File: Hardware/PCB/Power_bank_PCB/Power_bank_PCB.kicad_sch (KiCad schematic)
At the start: 0 parts

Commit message: Add battery protection and control schematic
Adds the custom 8205A MOSFET symbol and KiCad project metadata generated by the PCB editor, plus updates to the Power_bank_PCB schematic with the battery charger, protection, switching, MCU, and INA219 monitoring blocks. Also includes backup ZIPs and lockfile cleanup for the project.
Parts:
- added C1: C_Polarized, symbol Device:C_Polarized
- added C2: 0.1u, symbol Device:C
- added J1: Fotopanel_connector, symbol Connector:Screw_Terminal_01x02
- added Q1: 8205A, Package_SO:TSSOP-8_4.4x3mm_P0.65mm, symbol 8205A:8205A
- added Q2: 2N7002, Package_TO_SOT_SMD:SOT-23, symbol Transistor_FET:2N7002
- added Q3: DMP3099L, Package_TO_SOT_SMD:SOT-23, symbol Transistor_FET:DMP3099L
- added R1, R2: 10k, symbol Device:R
- added R3: 0.05, symbol Device:R
- added TP1: SWDIO, Connector_Pin:Pin_D1.3mm_L11.0mm_LooseFit, symbol Connector:TestPoint
- added TP2: SWCLK, Connector_Pin:Pin_D1.3mm_L11.0mm_LooseFit, symbol Connector:TestPoint
- added U1: TP4056-42-ESOP8, Package_SO:SOIC-8-1EP_3.9x4.9mm_P1.27mm_EP2.41x3.3mm_ThermalVias, symbol Battery_Management:TP4056-42-ESOP8
- added U2: XL4015, Package_TO_SOT_SMD:TO-263-5_TabPin3, symbol Regulator_Switching:XL4015
- added U3: MCP4018-xxxxLT, Package_TO_SOT_SMD:SOT-363_SC-70-6, symbol Potentiometer_Digital:MCP4018-xxxxLT
- added U4: DW01A, Package_TO_SOT_SMD:SOT-23-6, symbol Battery_Management:DW01A
- added U5: STM32U031F8Px, Package_SO:TSSOP-20_4.4x6.5mm_P0.65mm, symbol MCU_ST_STM32U0:STM32U031F8Px
- added U6: INA219AxD, Package_SO:SOIC-8_3.9x4.9mm_P1.27mm, symbol Sensor_Energy:INA219AxD
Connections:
- new net: Q3.2 (S), R2.1, R3.2, U6.7 (IN-)
- new net: J1.2 (Pin_2), R3.1, U6.8 (IN+)
- new net: TP1.1, U5.17 (PA13)
- new net: Q2.3 (D), Q3.1 (G), R2.2
- new net: TP2.1, U5.18 (PA14/PB4/PB5/PB6)
- new net +3.3V: C2.2, U6.5 (VS)
- new net Fotopanel_switch: Q2.1 (G), R1.1
- new net GND: C2.1, J1.1 (Pin_1), Q2.2 (S), R1.2, U6.1 (A1), U6.2 (A0), U6.6 (GND)
- new net SCL: U6.4 (SCL)
- new net SDA: U6.3 (SDA)
- new net Vfoto: Q3.3 (D)

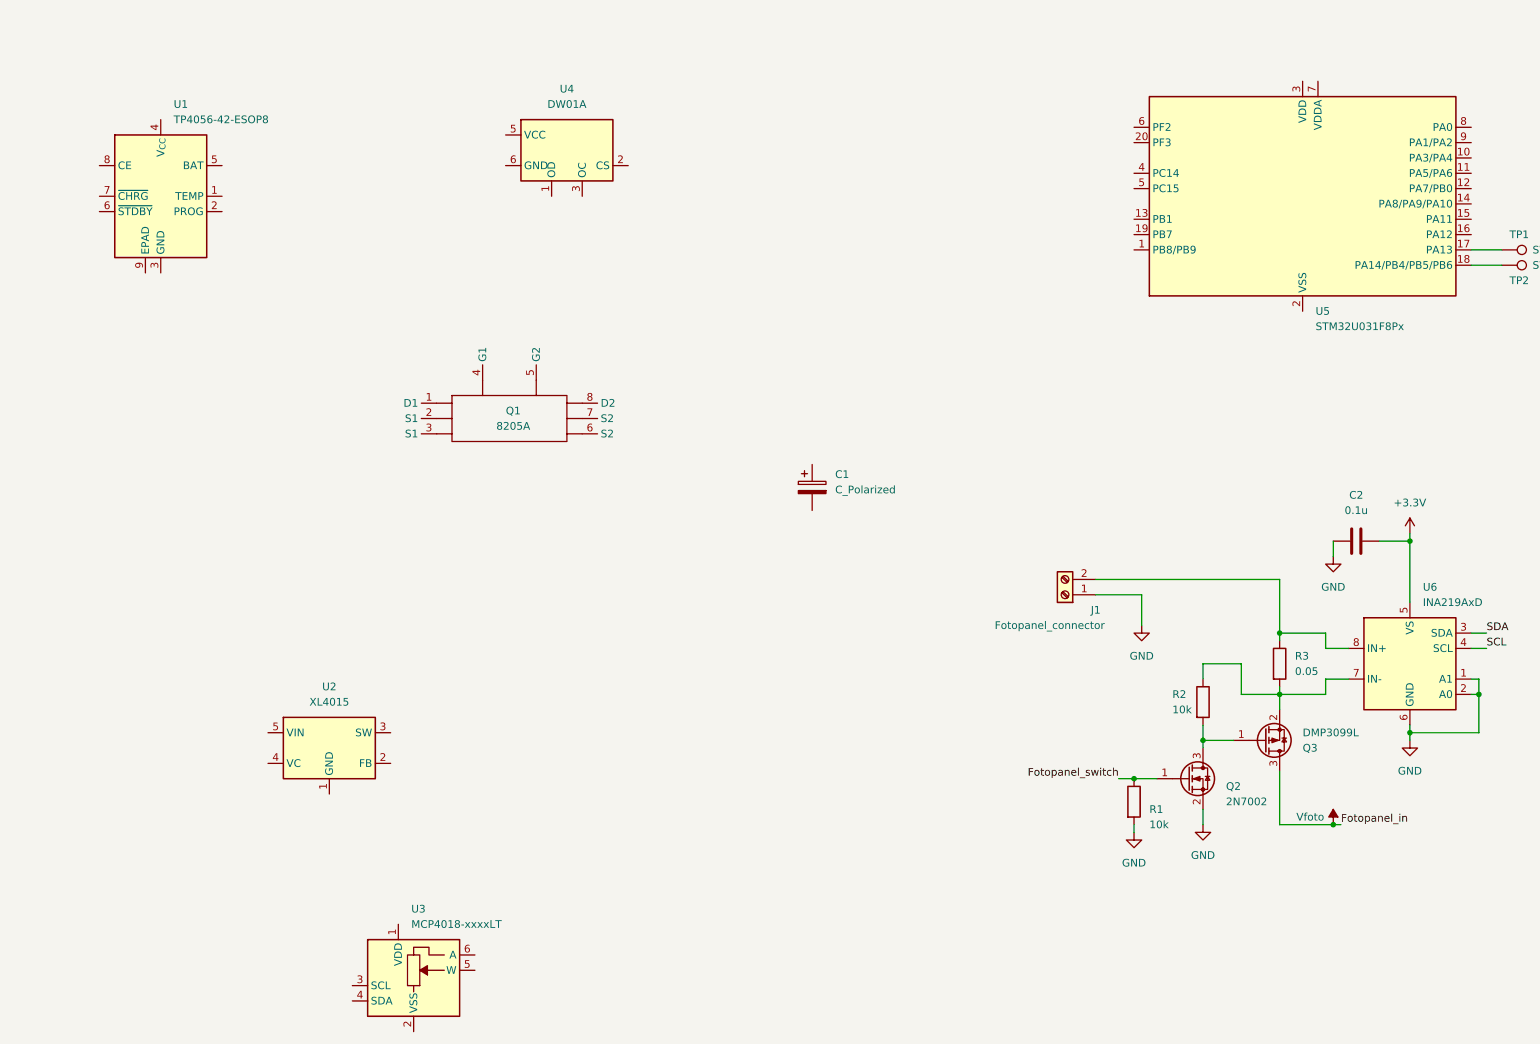
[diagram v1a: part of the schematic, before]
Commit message: Update of BMS, not finished
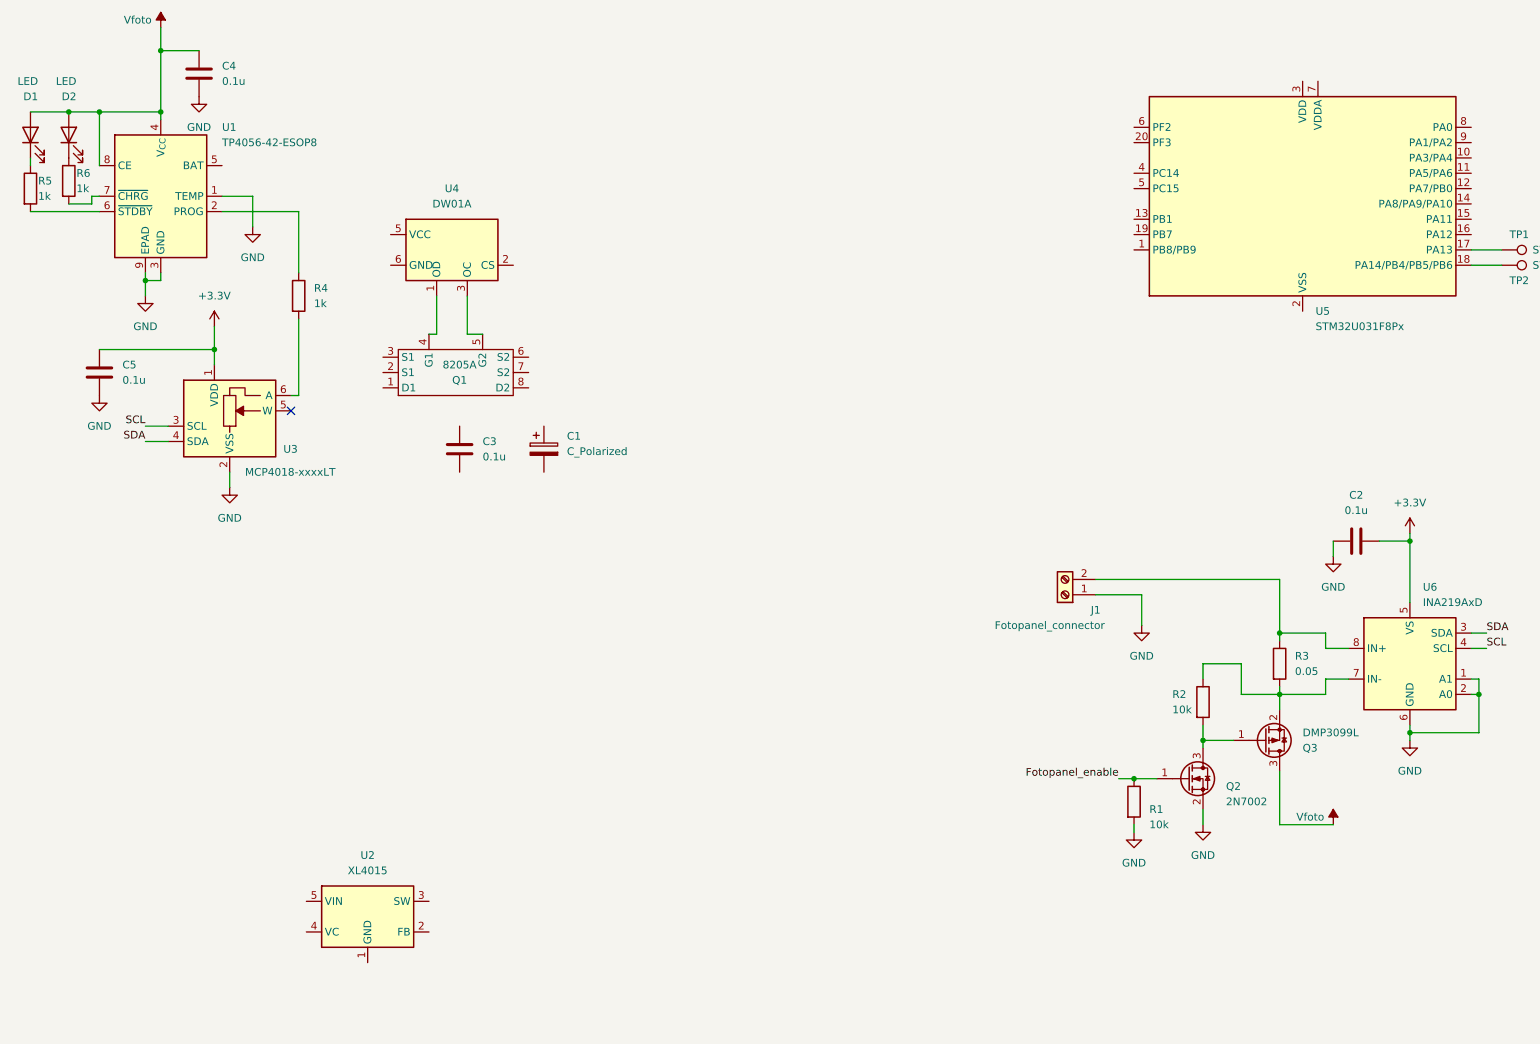
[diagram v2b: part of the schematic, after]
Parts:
- added C3, C4, C5: 0.1u, symbol Device:C
- added D1, D2: LED, symbol Device:LED
- added R4, R5, R6: 1k, symbol Device:R
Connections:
- net +3.3V: now also U3.1 (VDD), C5.1
- net GND: now also U1.1 (TEMP), U1.3 (GND), U1.9 (EPAD), U3.2 (VSS), C4.2, C5.2
- net SCL: now also U3.3 (SCL)
- net SDA: now also U3.4 (SDA)
- net Vfoto: now also U1.4 (V_{CC}), U1.8 (CE), C4.1, D1.2 (A), D2.2 (A)
- net at U4.1 (OD): now also Q1.4 (G1)
- net at U4.3 (OC): now also Q1.5 (G2)
- net at U1.2 (PROG): now also R4.1
- net at U1.6 (~{STDBY}): now also R5.2
- net at U1.7 (~{CHRG}): now also R6.2
- net at U3.6 (A): now also R4.2
- net Fotopanel_switch renamed Fotopanel_enable
- new net: D1.1 (K), R5.1
- new net: D2.1 (K), R6.1
- no-connect marks 0 -> 1
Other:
- moved on the sheet: C1, U2, U3, U4

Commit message: Update of schematic
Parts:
- removed U2: XL4015, Package_TO_SOT_SMD:TO-263-5_TabPin3, symbol Regulator_Switching:XL4015
- added C6: 680u, symbol Device:C_Polarized
- added C7: 0.1u, symbol Device:C
- added C8: 22u, symbol Device:C
- added C9: 220u, symbol Device:C_Polarized
- added D3: SS23, Diode_SMD:D_SMA, symbol Diode:SS23
- added L1: 33uH / 3A, symbol Device:L
- added L2: 4.7uH / 1.5A, symbol Device:L
- added R7: 100, symbol Device:R
- added R8: 1k, symbol Device:R
- added TP3: Vbat, Connector_Pin:Pin_D1.3mm_L11.0mm_LooseFit, symbol Connector:TestPoint
- added TP4: Bat-, Connector_Pin:Pin_D1.3mm_L11.0mm_LooseFit, symbol Connector:TestPoint
- added U7: LM2596S-5, Package_TO_SOT_SMD:TO-263-5_TabPin3, symbol Regulator_Switching:LM2596S-5
- added U8: TPS613221ADBV, Package_TO_SOT_SMD:SOT-23-5, symbol Regulator_Switching:TPS613221ADBV
- C1: value C_Polarized -> 10u
- C4: value 0.1u -> 10u
- R4: value 1k -> 3k
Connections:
- net +3.3V: now also C8.1, U8.4 (VOUT)
- net GND: now also C1.2, Q1.6 (S2), Q1.7 (S2), U3.5 (W), C6.2, C7.2, C8.2, C9.2, D3.2 (A), R8.2, U7.3 (GND), U7.5 (~{ON}/OFF), U8.2 (GND)
- net Vfoto: now also C6.1, C7.1, U7.1 (VIN); no longer C4.1, D1.2 (A), D2.2 (A), U1.4 (V_{CC}), U1.8 (CE)
- net at U4.2 (CS): now also R8.1
- net at U4.5 (VCC): now also C3.2, R7.2
- net Bat-: now reaches U4.6 (GND)
- net Bat-: now also C3.1, Q1.2 (S1), Q1.3 (S1), TP4.1
- net Vbat: now reaches U1.5 (BAT)
- net Vbat: now also C1.1, L2.1, R7.1, TP3.1
- net at Q1.1 (D1): now also Q1.8 (D2)
- new net: D3.1 (K), L1.1, U7.2 (OUT)
- new net: L2.2, U8.1 (SW)
- new net Vcharge: C4.1, C9.1, D1.2 (A), D2.2 (A), L1.2, U1.4 (V_{CC}), U1.8 (CE), U7.4 (FB)
- no-connect marks 1 -> 0
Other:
- note added: "find and replace to buck-boost converter!!"
- moved on the sheet: C1, C2, C3, J1, Q1, Q2, Q3, R1, R2, R3, U4, U6

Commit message: Finishing schematic
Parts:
- removed C6: 680u, symbol Device:C_Polarized
- removed C8: 22u, symbol Device:C
- removed C9: 220u, symbol Device:C_Polarized
- removed D3: SS23, Diode_SMD:D_SMA, symbol Diode:SS23
- removed U7: LM2596S-5, Package_TO_SOT_SMD:TO-263-5_TabPin3, symbol Regulator_Switching:LM2596S-5
- removed U8: TPS613221ADBV, Package_TO_SOT_SMD:SOT-23-5, symbol Regulator_Switching:TPS613221ADBV
- added C10, C12, C14, C3, C5: 22u, symbol Device:C
- added C13, C15, C16, C17, C18, C19, C20, C6: 10u, symbol Device:C
- added C2, C21, C22, C23, C9: 100n, symbol Device:C
- added C24: 4.7u, symbol Device:C
- added C25: 1u, symbol Device:C
- added C26: 10n, symbol Device:C
- added IC1, IC2: TPS63070RNMR, KiCad:TPS630701RNMR, symbol TPS63070RNMR:TPS63070RNMR
- added R10, R15, R6: 10k, symbol Device:R
- added R12, R16, R17: 470k, symbol Device:R
- added R13: 150k, symbol Device:R
- added R14, R8: 100k, symbol Device:R
- added R3: 680k, symbol Device:R
- added R4: 130k, symbol Device:R
- added R7: 20k, symbol Device:R
- added TP10: User_button+, Connector_Pin:Pin_D1.3mm_L11.0mm_LooseFit, symbol Connector:TestPoint
- added TP3: Green_LED, Connector_Pin:Pin_D1.3mm_L11.0mm_LooseFit, symbol Connector:TestPoint
- added TP4: Leds_common_GND, Connector_Pin:Pin_D1.3mm_L11.0mm_LooseFit, symbol Connector:TestPoint
- added TP5: User_button-, Connector_Pin:Pin_D1.3mm_L11.0mm_LooseFit, symbol Connector:TestPoint
- added TP8: Red_LED, Connector_Pin:Pin_D1.3mm_L11.0mm_LooseFit, symbol Connector:TestPoint
- added TP9: Yellow_LED, Connector_Pin:Pin_D1.3mm_L11.0mm_LooseFit, symbol Connector:TestPoint
- L1: value 33uH / 3A -> 1.5uH
- L2: value 4.7uH / 1.5A -> 1.5uH
- renumbered C5 to C1, C1 to C11, C2 to C27, C3 to C8, R5 to R1, R8 to R11, R1 to R18, R2 to R19, R6 to R2, R3 to R20, R4 to R5, R7 to R9, TP4 to TP1, TP3 to TP2, TP1 to TP6, TP2 to TP7, U3 to U2, U4 to U3, U5 to U4, U6 to U5
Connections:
- net +3.3V: now also U4.3 (VDD), U4.7 (VDDA), C10.2, C12.2, C14.2, C17.2, C21.2, C22.2, C23.2, C24.2, C25.2, C26.2, IC2.7 (VOUT_1), IC2.8 (VOUT_2), R12.1, R14.2, R16.1, R17.1
- net Fotopanel_enable: now also U4.10 (PA3/PA4)
- net GND: now also U4.2 (VSS), C10.1, C12.1, C13.1, C14.1, C15.1, C16.1, C17.1, C18.1, C19.1, C2.1, C20.1, C21.1, C22.1, C23.1, C24.1, C25.1, C26.1, C3.1, C5.1, C6.1, C9.1, IC1.10 (PGND), IC1.15 (VSEL), IC1.4 (GND), IC1.6 (FB2), IC2.10 (PGND), IC2.15 (VSEL), IC2.4 (GND), IC2.6 (FB2), R13.2, R4.2, R7.2, TP4.1, TP5.1
- net SCL: now also U4.19 (PB7), R17.2
- net SDA: now also U4.1 (PB8/PB9), R16.2
- net Vbat: now also C18.2, C19.2, C20.2, IC2.12 (VIN_1), IC2.13 (VIN_2), R15.1, R6.1; no longer L2.1
- net Vcharge: now also C3.2, C5.2, C6.2, IC1.7 (VOUT_1), IC1.8 (VOUT_2), R3.1, R8.2; no longer L1.2
- net Vfoto: now also C13.2, C15.2, C16.2, IC1.12 (VIN_1), IC1.13 (VIN_2), R10.1; no longer C7.1
- net at L1.1: now also IC1.9 (L2)
- net at U4.11 (PA5/PA6): now also TP8.1
- net at U4.12 (PA7/PB0): now also TP9.1
- net at U4.13 (PB1): now also TP3.1
- net at U4.14 (PA8/PA9/PA10): now also TP10.1
- net Battery_state: now reaches U4.8 (PA0)
- net Battery_state: now also C7.1, R6.2, R7.1
- net at L2.2: now also IC2.11 (L1)
- new net: IC2.1 (PS/S), IC2.14 (EN), R15.2
- new net: IC1.5 (FB), R3.2, R4.1
- new net: IC1.1 (PS/S), IC1.14 (EN), R10.2
- new net: IC1.11 (L1), L1.2
- new net: IC1.2 (PG), R8.1
- new net: C2.2, IC1.3 (VAUX)
- new net: IC2.9 (L2), L2.1
- new net: IC2.5 (FB), R12.2, R13.1
- new net: C9.2, IC2.3 (VAUX)
- new net: IC2.2 (PG), R14.1
- no-connect marks 0 -> 6
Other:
- note removed: "find and replace to buck-boost converter!!"
- moved on the sheet: C1, C11, C27, C4, C8, D1, D2, J1, L1, Q1, Q2, Q3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

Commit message: Added two USB, as power output and alternative power input
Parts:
- added D3: D_Schottky, symbol Device:D_Schottky
- added J2: Vout, Connector_USB:USB_A_Molex_67643_Horizontal, symbol Connector:USB_A
- added J3: Alterative_charging, Connector_USB:USB_C_Receptacle_GCT_USB4125-xx-x-0190_6P_TopMnt_Horizontal, symbol Connector:USB_C_Receptacle_PowerOnly_6P
- added L3: 10u, symbol Device:L
- added Q4: DMG2301L, Package_TO_SOT_SMD:SOT-23, symbol Transistor_FET:DMG2301L
- added R21, R22: 5.1k, symbol Device:R
- added R23, R24: 10k, symbol Device:R
- added U6: LTC3525-5, Package_TO_SOT_SMD:SOT-363_SC-70-6, symbol Regulator_Switching:LTC3525-5
- R16, R17: value 470k -> 4.7k
- R6: value 10k -> 100k
- R7: value 20k -> 200k
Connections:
- net +3.3V: now also R24.1
- net GND: now also J2.4 (GND), J2.SH (Shield), J3.A12 (GND), J3.B12 (GND), J3.SH (SHIELD), R21.2, R22.2, R23.2, U6.2 (GND), U6.5 (GND)
- net Vbat: now also L3.1, U6.3 (VIN)
- net Vcharge: now also Q4.3 (D); no longer C4.1, D1.2 (A), D2.2 (A), U1.4 (V_{CC}), U1.8 (CE)
- new net: R24.2, U6.1 (~{SHDN})
- new net: L3.2, U6.6 (SW)
- new net: J3.B5 (CC2), R21.1
- new net: D3.2 (A), J3.A9 (VBUS), J3.B9 (VBUS), R23.1
- new net 5V: J2.1 (VBUS), U6.4 (VOUT)
- new net Vbus: C4.1, D1.2 (A), D2.2 (A), D3.1 (K), Q4.1 (G), Q4.2 (S), U1.4 (V_{CC}), U1.8 (CE)
- no-connect marks 6 -> 8
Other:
- moved on the sheet: C4

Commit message: Add R25/R26, USB_FLAG label and power symbol
Update KiCad schematic and project to add two resistors (R25, R26), a new power net symbol (#PWR062), USB_FLAG labels, and related wires/junctions. Also update used_designators in Power_bank_PCB.kicad_pro. Files changed: Hardware/PCB/Power_bank_PCB/Power_bank_PCB.kicad_sch and Power_bank_PCB.kicad_pro. These edits place the new components and adjust wiring to connect them in the schematic.
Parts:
- added R25: 10k, symbol Device:R
- added R26: 20k, symbol Device:R
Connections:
- net GND: now also R26.2
- net at D3.2 (A), J3.A9 (VBUS), J3.B9 (VBUS)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: now also R25.1
- net USB_FLAG: now reaches U4.4 (PC14)
- net USB_FLAG: now also R25.2, R26.1

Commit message: Update PCB schematic: add TPS61022 & INA219
Introduce TPS61022 boost-converter symbol and replace the LTC3525 entry with an INA219 energy/current-sense symbol (value, footprint and datasheet updated). Swap/rename several parts (FET -> DMP3099L), add global power symbols (+3.3V, +5V, VBUS, GND, Vbat), testpoints and discrete components (R24, R27, R16, R19, C10u, D4), and reorganize many wires/junctions and component positions. Also update Power_bank_PCB.kicad_pro used_designators to reflect added/renamed components. These changes align schematic symbols, footprints and net connections with the updated design.
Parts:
- removed Q4: DMG2301L, Package_TO_SOT_SMD:SOT-23, symbol Transistor_FET:DMG2301L
- removed U6: LTC3525-5, Package_TO_SOT_SMD:SOT-363_SC-70-6, symbol Regulator_Switching:LTC3525-5
- added C10u: 22u, symbol Device:C
- added D4: D_Schottky, symbol Device:D_Schottky
- added R27: 100k, symbol Device:R
- added U6: TPS61022, Package_DFN_QFN:Texas_RWU0007A_VQFN-7_2x2mm_P0.5mm, symbol Converter_DCDC:TPS61022
- L3: value 10u -> 4.7u
- R24: value 10k -> 732k
- R25: value 10k -> 22k
- R26: value 20k -> 33k
- R5: value 3k -> 2k
- R6: value 100k -> 220k
- R7: value 200k -> 330k
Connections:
- net +3.3V: no longer R24.1
- net 5V: now also R24.1, U6.3 (VOUT)
- net GND: now also C10u.1, R27.2, U6.1 (GND)
- net Vbat: now also C10u.2, U6.5 (EN), U6.6 (MODE), U6.7 (VIN)
- net Vbus: now also D4.1 (K)
- net Vcharge: now also D4.2 (A)
- net at R24.2: now also R27.1
- net at L3.2: now also U6.2 (SW)
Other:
- moved on the sheet: J2, L3, R23
